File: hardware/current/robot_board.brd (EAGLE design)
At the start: 95.2 x 76.1 mm, 150 parts, among them J1 POWER_JACKPTH, Q1 DMP2035U, Q2 DMP2035U, Q3 DMP2035U-7, Q4 DMP2035U-7, Q5 DMP2035U, U1 FT232RL-BASICSSOP, U10 DRV8839, U12 LM393, U16 LM393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

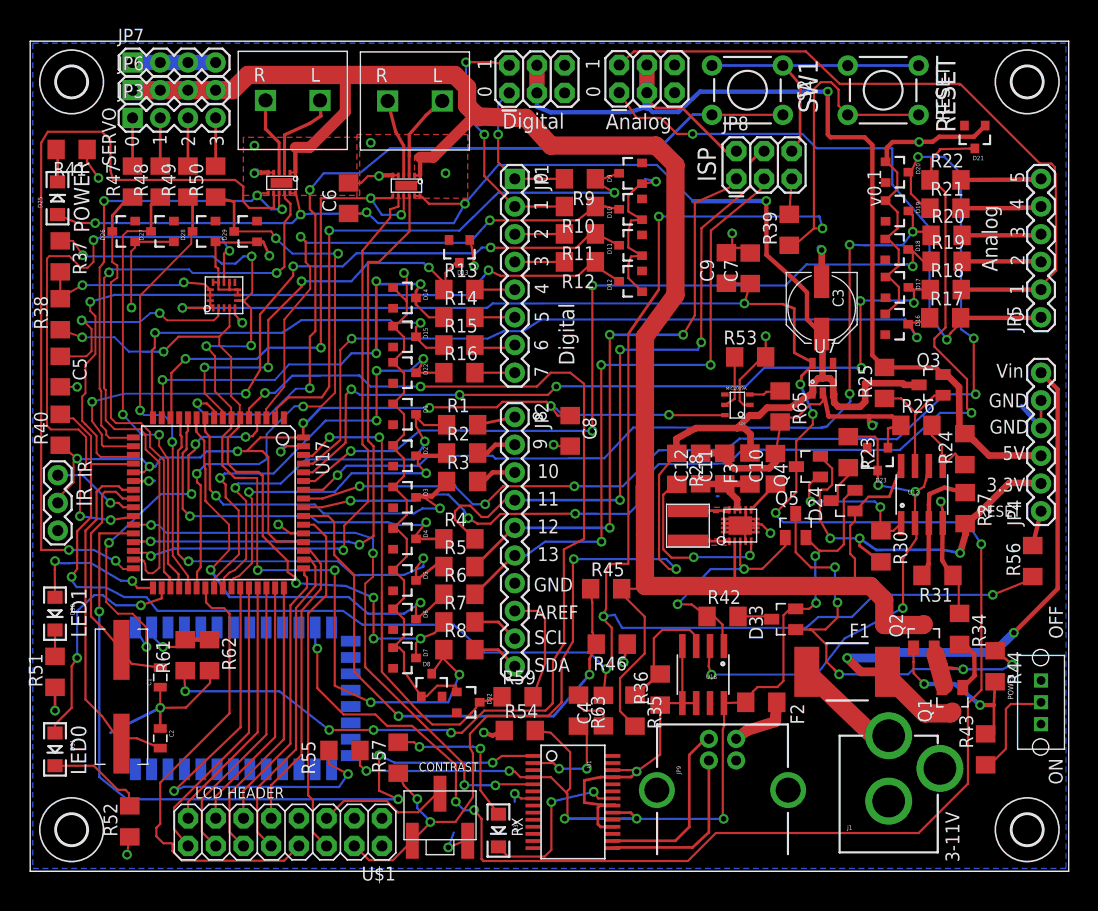
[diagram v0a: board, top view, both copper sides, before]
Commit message: USB and main power are switched with on/off switch
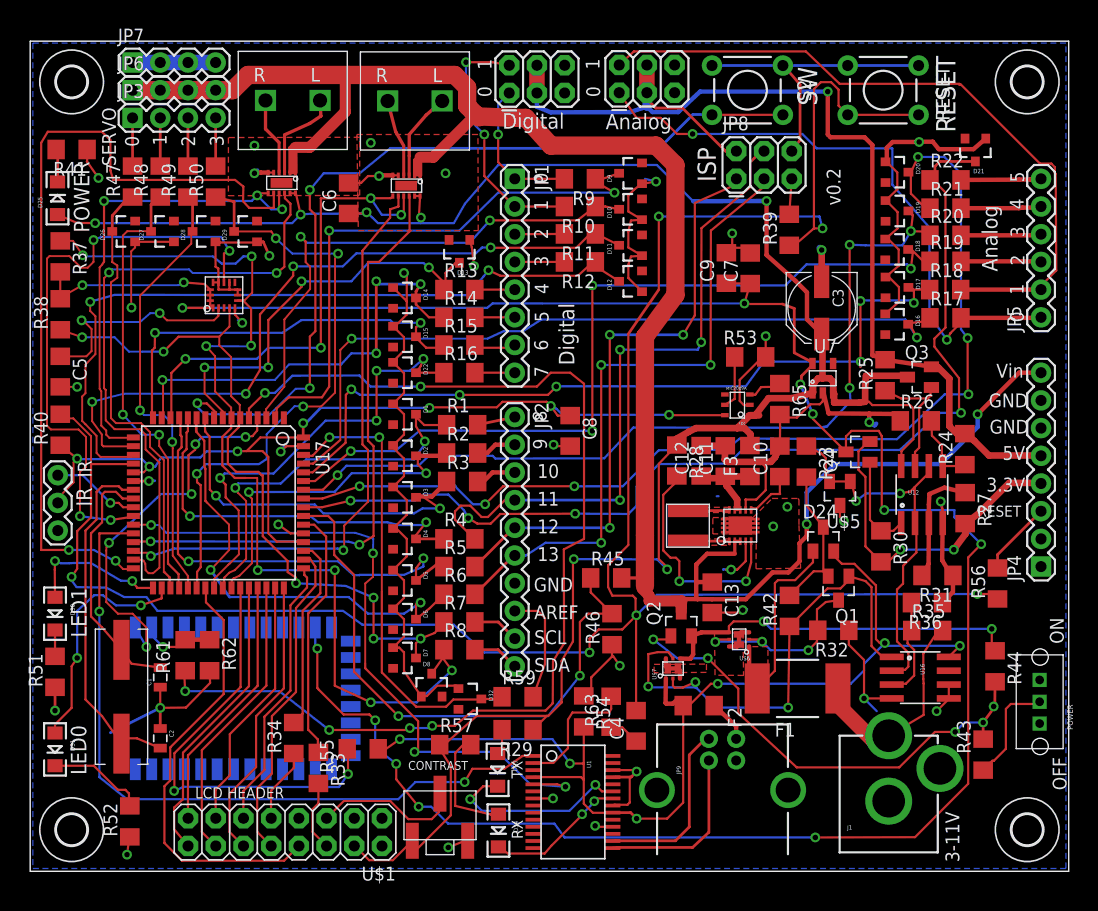
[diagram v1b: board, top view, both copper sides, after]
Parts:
- removed D33: BAT54C, diode:SOT23
- removed Q5: DMP2035U, jseng:SOT23
- added C13: 22uF, resistor:C1206
- added R29: 330, resistor:R1206
- added R32: 20K 1%, resistor:R1206
- added R33: 300, resistor:R1206
- added U$5: AP431SAG-7, jseng:SOT23
- added U$6, U$7: SIA907EDJT, jseng:SC70T
- D23: value 2.4V -> RX; device SparkFun-DiscreteSemi:SOT23-3 -> SparkFun-LED:LED-1206
- JP4: device SparkFun-Connectors:1X06 -> SparkFun-Connectors:1X08
- R23: value 1K 1% -> 10K 1%
- R24: value 27K 1% -> 24K 1%
- R31: value 20K 1% -> 24K 1%
- R34: value 20K 1% -> 300
- R35: value 5.11K 1% -> 120K 1%
- R36: value 20K 1% -> 600K 1%
- moved R34 61.9 mm to (24.2, 12.2), turned to 90 degrees
- moved D23 45.1 mm to (42.9, 9.30), turned to 270 degrees
- moved R35 27.8 mm to (82.3, 22.1), turned to 0 degrees
- moved R36 25.7 mm to (82.2, 24.6), turned to 180 degrees
- moved Q2 22.3 mm to (59.7, 22.7)
- moved U16 19.9 mm to (81.6, 17.8), turned to 270 degrees
- moved Q1 14.6 mm to (74.1, 26.0)
- moved R42 6.17 mm to (69.6, 23.9), turned to 90 degrees
- moved R54 6.12 mm to (50.8, 14.7), turned to 270 degrees
- moved F2 5.75 mm to (61.3, 15.2)
- moved R57 5.37 mm to (39.0, 11.6), turned to 0 degrees
- moved JP4 5.08 mm to (92.7, 27.9)
- moved F1 4.80 mm to (70.4, 16.8), turned to 180 degrees
- moved Q4 4.74 mm to (75.9, 38.5)
- moved D24 3.96 mm to (72.7, 30.5), turned to 0 degrees
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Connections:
- removed net 2.4V: D23.3, R23.1, U12.2, U12.6, U16.2
- removed net N$33: F1.2, JP4.6, Q1.3
- removed net N$36: Q1.1, R34.2
- new net 2.5V: R23.1, U$5.1, U$5.2, U12.2, U12.6, U16.2
- new net N$22: D23.C, U1.23
- new net N$23: U$7.D1@1, U$7.D1@2, U$7.D2@1, U$7.D2@2
- new net N$24: U$6.D1@1, U$6.D1@2, U$6.D2@1, U$6.D2@2
- new net N$25: R33.2, U$1.6
- new net N$26: R34.1, U$1.9
- new net PWR_GATE: Q1.3, R32.2, U$6.G1, U$6.G2
- new net VIN1: D24.1, F1.2, U$6.S1
- net 3V3_OUT: now also JP4.4; no longer JP4.2
- net 5V: now also R29.1, U12.8
- net 5V_OUT: now also JP4.5; no longer JP4.3
- net GND: now also C13.2, JP4.6, JP4.7, R32.1, U$5.3; no longer D23.1, JP4.4, JP4.5, R34.1
- net LCD0: now also R34.2; no longer U$1.9
- net N$12: now also D23.A, R29.2; no longer D33.3, R42.2
- net N$18: now also Q1.2, R42.2
- net N$7: now also JP4.3; no longer JP4.1
- net PWR_SW: now also U$6.S2, U$7.S2; no longer D33.1, Q1.2, Q5.3
- net RS: now also R33.1; no longer U$1.6
- net USBGATE: now also Q1.1, U$7.G1, U$7.G2; no longer Q5.1, U$3.P$3
- net USB_5V: now also U$7.S1; no longer D33.2, Q5.2
- net VIN: now also R35.2
- net VIN_F: now also C13.1, JP4.8, U$3.P$3; no longer D24.1, R35.2, U12.8
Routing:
- net N$33: track 54.4 -> 0.00 mm, vias 2 -> 0
- net 2.4V: track 47.8 -> 0.00 mm, vias 4 -> 0
- net 2.5V: track 0.00 -> 36.6 mm, vias 0 -> 2
- net N$51: track 16.3 -> 45.9 mm, vias 2 -> 5
- net USBGATE: track 22.4 -> 47.8 mm, vias 2 -> 3
- net VIN1: track 0.00 -> 19.8 mm
- net PWR_GATE: track 0.00 -> 18.0 mm, vias 0 -> 3
- net N$22: track 0.00 -> 17.8 mm, vias 0 -> 2
- net PWR_SW: track 46.6 -> 33.9 mm, vias 5 -> 2
- net N$18: track 3.98 -> 13.8 mm
- net LCD0: track 27.4 -> 17.9 mm
- net VIN: track 11.0 -> 20.0 mm
- net RS: track 32.3 -> 23.4 mm
- net GND: track 325.4 -> 317.3 mm, vias 32 -> 38
- net TX: track 55.5 -> 62.6 mm
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- added copper zone on layer 1, net N$23
- added copper zone on layer 1, net N$24
- added copper zone on layer 1, net VIN1
- removed copper zone on layer 1, net VIN_F
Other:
- board text added: "SW"
- board text added: "TX"
- board text added: "v0.2"
- board text removed: "SW1"
- board text removed: "v0.1"

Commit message: before adding 5V i2c resistors
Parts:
- moved C1 0.51 mm to (11.9, 18.3)
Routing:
- net GND: track 317.3 -> 314.3 mm
- net SDA_IN: track 91.3 -> 88.4 mm
- net RESET: track 205.3 -> 203.1 mm
- net VIN_F: track 189.2 -> 187.6 mm
- net PWR_GATE: track 18.0 -> 19.5 mm
- net D4_IN: track 39.1 -> 40.5 mm
- net D2_IN: track 66.5 -> 67.9 mm
- net D13: track 59.1 -> 60.5 mm
- net D11: track 61.8 -> 63.1 mm
- net D1_IN: track 49.2 -> 50.2 mm
- net BT_RX: track 102.7 -> 103.7 mm
- net D3_IN: track 70.8 -> 71.6 mm
- net 5V: track 207.7 -> 207.1 mm
- net N$8: track 20.4 -> 19.9 mm
- added copper zone on layer 1, net VIN_F
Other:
- board text added: "LED2"
- board text removed: "LED0"

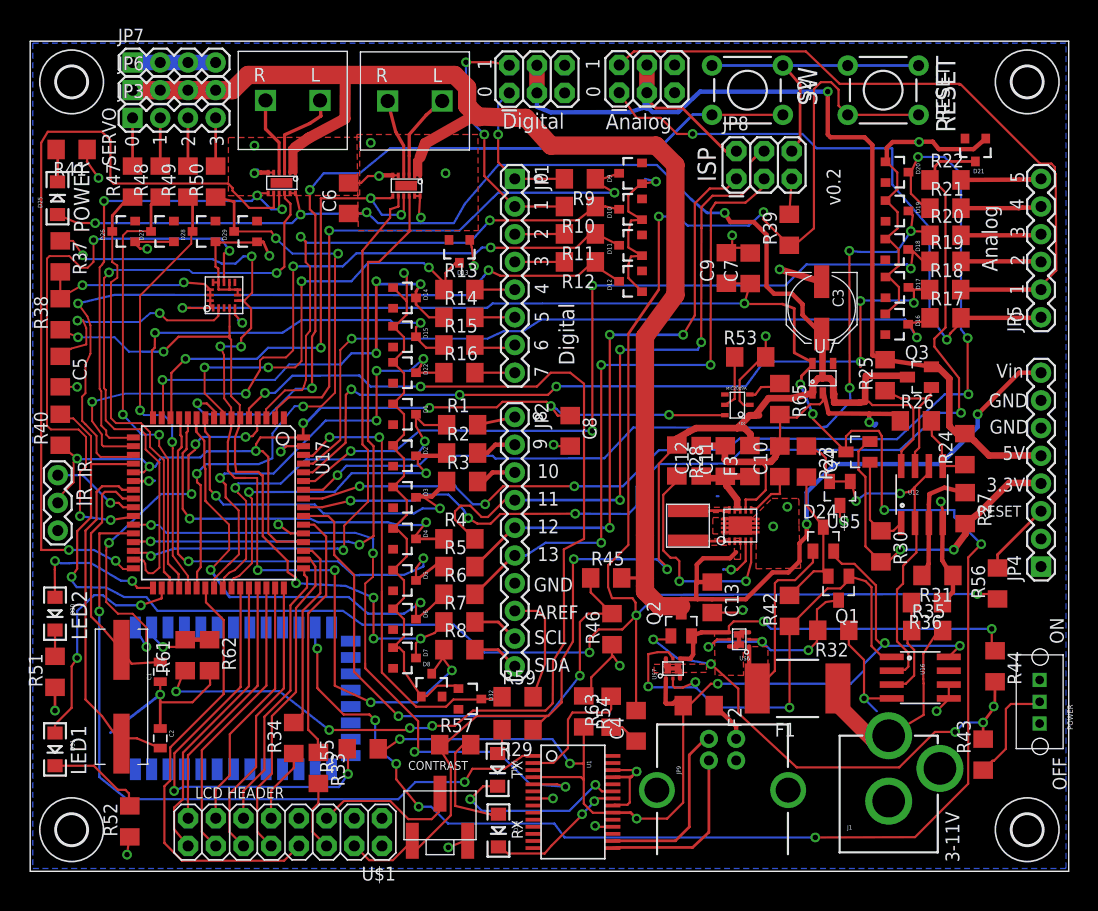
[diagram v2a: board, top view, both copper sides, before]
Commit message: added i2c level shifter
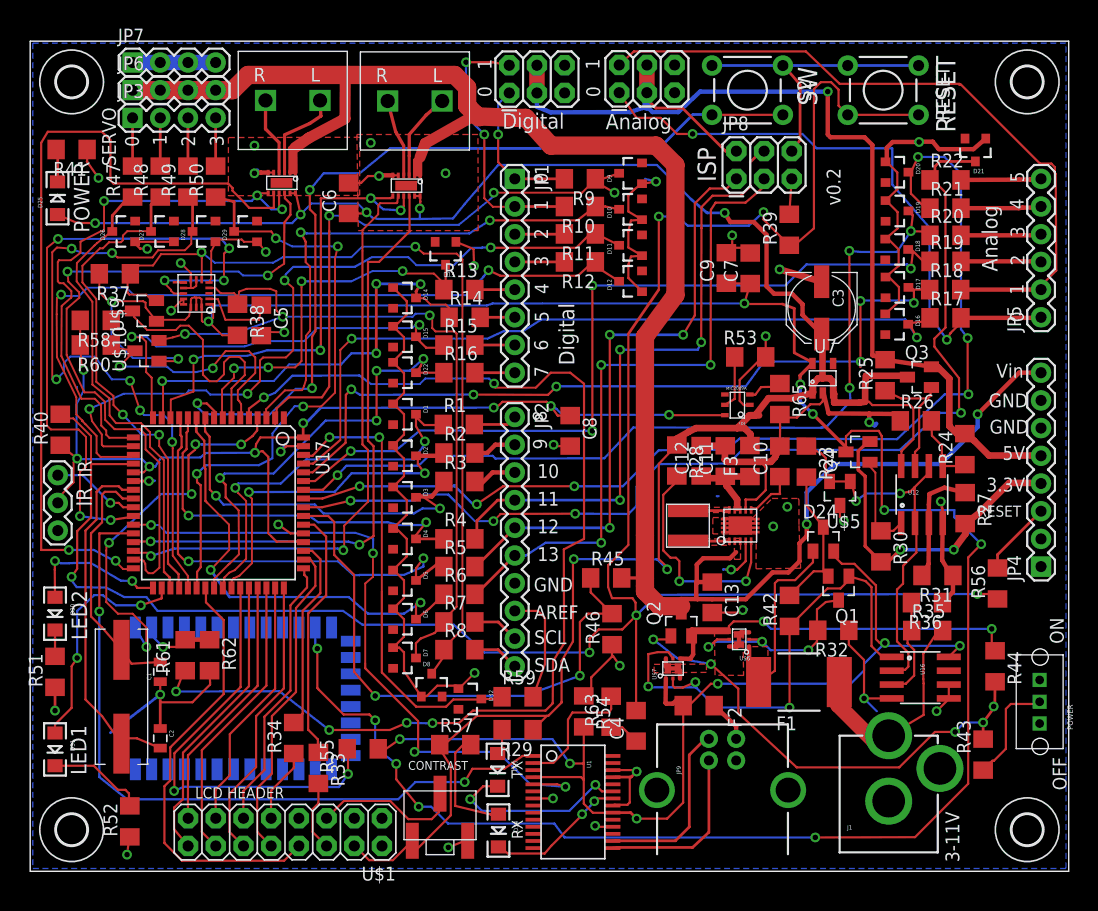
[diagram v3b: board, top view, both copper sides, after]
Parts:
- added R58, R60: 10K 1%, resistor:R1206
- added U$10, U$9: BSS138, jseng:SOT23
- R37, R38: value 4.7K -> 10K 1%
- moved C5 19.0 mm to (21.2, 50.5)
- moved R38 16.3 mm to (19.0, 50.6), turned to 270 degrees
- moved R37 5.25 mm to (7.77, 54.8), turned to 180 degrees
- moved U$8 2.54 mm to (15.2, 53.0), turned to 180 degrees
- moved D13 1.28 mm to (38.1, 56.7)
- moved F1 0.60 mm to (70.5, 17.3)
- moved R14 0.48 mm to (39.9, 50.8)
- moved R1 0.31 mm to (39.3, 41.0)
- moved R2 0.25 mm to (39.4, 38.4)
- moved R3 0.25 mm to (39.4, 35.7)
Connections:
- new net SCL_5V: R60.1, U$10.3, U17.6
- new net SDA_5V: R58.1, U$9.3, U17.7
- net 3V3: now also U$10.1, U$9.1
- net 5V_UC: now also R58.2, R60.2
- net SCL_IN: now also U$10.2; no longer U17.6
- net SDA_IN: now also U$9.2; no longer U17.7
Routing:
- net SDA_5V: track 0.00 -> 25.4 mm
- net SCL_5V: track 0.00 -> 24.6 mm, vias 0 -> 2
- net SERVO2_IN: track 41.0 -> 61.7 mm, vias 2 -> 6
- net 5V_UC: track 86.9 -> 100.0 mm, vias 7 -> 8
- net 3V3: track 219.2 -> 232.0 mm
- net N$8: track 19.9 -> 7.29 mm, vias 2 -> 0
- net SDA_IN: track 88.4 -> 79.1 mm, vias 8 -> 2
- net M1_DIR0: track 57.9 -> 64.0 mm
- net ACCEL_INT: track 55.2 -> 61.3 mm, vias 4 -> 6
- net M1_EN: track 44.3 -> 50.1 mm
- net SCL_IN: track 66.8 -> 71.4 mm, vias 6 -> 3
- net D4_IN: track 40.5 -> 36.1 mm
- net D11: track 63.1 -> 59.1 mm
- net SERVO1_IN: track 41.8 -> 45.7 mm
- net PWR_SW: track 33.9 -> 37.6 mm
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
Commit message: revision 2
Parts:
- added JP12: M02PTH, SparkFun-Connectors:1X02
- added U$11: BSS138, jseng:SOT23
- R23: value 10K 1% -> 20K 1%
- U$1: value M08X2 -> 2X7HEADER; device SparkFun-Connectors:2X8 -> jseng:2X7
- moved D22 3.26 mm to (31.4, 47.2), turned to 180 degrees
- moved D1 2.86 mm to (36.9, 43.1), turned to 180 degrees
- moved U$1 2.55 mm to (29.7, 4.88)
- moved U$2 1.58 mm to (36.0, 2.77)
- moved D24 1.07 mm to (73.8, 30.5)
- moved R57 0.76 mm to (38.2, 11.6)
- moved U$20 0.76 mm to (22.4, 70.7)
- moved R1 0.74 mm to (40.0, 41.2)
- moved D34 0.51 mm to (42.4, 3.78)
- moved U$19 0.43 mm to (32.4, 70.7)
- moved D23 0.43 mm to (42.4, 9.30)
- moved D15 0.36 mm to (34.6, 49.0)
- moved D26 0.05 mm to (8.64, 58.7)
- moved D27 0.05 mm to (12.2, 58.7)
- moved D28 0.05 mm to (16.0, 58.7)
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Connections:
- new net ACCEL_INT1: U$11.1, U$8.P$11
- net 5V: now also U$1.2; no longer U$1.4
- net 5V_OUT: now also JP4.2
- net ACCEL_INT: now also U$11.3; no longer U$8.P$11
- net E: now also U$1.6; no longer U$1.8
- net GND: now also U$1.1, U$1.5, U$11.2; no longer U$1.3, U$1.7
- net LCD1: now also U$1.8; no longer U$1.10
- net LCD2: now also U$1.9; no longer U$1.11
- net LCD3: now also U$1.10; no longer U$1.12
- net LCD4: now also U$1.11; no longer U$1.13
- net LCD5: now also U$1.12; no longer U$1.14
- net LCD6: now also U$1.13; no longer U$1.15
- net LCD7: now also U$1.14; no longer U$1.16
- net LED0: now also U17.34; no longer U17.33
- net LED1: now also U17.33; no longer U17.34
- net N$15: now also U$1.3; no longer U$1.5
- net N$25: now also U$1.4; no longer U$1.6
- net N$26: now also U$1.7; no longer U$1.9
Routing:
- net D1: track 24.8 -> 40.8 mm
- net ACCEL_INT1: track 0.00 -> 12.1 mm, vias 0 -> 2
- net RESET: track 203.1 -> 195.4 mm
- net 5V_OUT: track 96.9 -> 103.2 mm
- net ACCEL_INT: track 61.3 -> 56.7 mm, vias 6 -> 4
- net GND: track 315.2 -> 319.4 mm, vias 39 -> 40
- net VIN_F: track 187.6 -> 190.2 mm
- net N$15: track 14.0 -> 11.4 mm
- net 5V: track 207.0 -> 204.7 mm
- net D7_IN: track 41.6 -> 39.6 mm, vias 4 -> 2
- net LED0: track 13.1 -> 14.9 mm
- net M1_DIR0: track 64.0 -> 65.7 mm
- net M0_DIR0: track 55.9 -> 57.6 mm
- net A1_IN: track 73.6 -> 75.1 mm
- net N$18: track 13.8 -> 15.3 mm
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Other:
- board text added: "LED0"
- board text added: "Motor 0"
- board text added: "Motor 1"
- board text removed: "LED2"
